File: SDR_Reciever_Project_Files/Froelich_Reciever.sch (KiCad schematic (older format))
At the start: 84 parts, among them J1 I_IN0, J10 LO_I, J11 4.3V, J12 CLK0, J13 RF_IN, J14 RF_OUT, J15 Antenna In, J16 CLK1, J17 CLK2, J18 Conn_01x02_Female, J19 Conn_01x02_Female, J2 I_AMP, J20 I_OUT, J21 Q_OUT, J3 I_IN180, J4 AudioJack3, J5 Q_IN90, J6 Q_AMP, J7 Q_IN270, J8 LO_Q, J9 5V, Q1 PN2222A, U1 INA821ID, U2 SN74CBT3253, U3 OP213FPZ, U4 INA821ID, U5 74AC74, U6 Si5351A-B-GT, U7 LM741, Y1 ATS250

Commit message: Updated footprint libraries, and netlist.
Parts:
- U1, U4: footprint INA821ID:SOIC127P600X175-8N -> Imported_Footprints:INA821ID
- U3: footprint footprints:OP213FPZ -> Imported_Footprints:OP213
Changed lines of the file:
@@
 F 0 "U4" H 5600 3350 50  0000 L CNN
 F 1 "INA821ID" H 5500 3250 50  0000 L CNN
-F 2 "INA821ID:SOIC127P600X175-8N" H 5750 3275 50  0001 L BNN
+F 2 "Imported_Footprints:INA821ID" H 5750 3275 50  0001 L BNN
 F 3 "B" H 5750 3275 50  0001 L BNN
 F 4 "1.75mm" H 5750 3275 50  0001 L BNN "Field4"
@@
 F 0 "U1" H 5600 1875 50  0000 L CNN
 F 1 "INA821ID" H 5500 1775 50  0000 L CNN
-F 2 "INA821ID:SOIC127P600X175-8N" H 5750 1800 50  0001 L BNN
+F 2 "Imported_Footprints:INA821ID" H 5750 1800 50  0001 L BNN
 F 3 "http://www.ti.com/general/docs/suppproductinfo.tsp?distId=10&gotoUrl=http%3A%2F%2Fwww.ti.com%2Flit%2Fgpn%2Fina821" H 5750 1800 50  0001 L BNN
 F 4 "1.75mm" H 5750 1800 50  0001 L BNN "Field4"
@@
 F 0 "U3" H 8600 2375 60  0000 C CNN
 F 1 "OP213FPZ" H 8600 2275 60  0000 C CNN
-F 2 "footprints:OP213FPZ" H 8525 2625 60  0001 C CNN
+F 2 "Imported_Footprints:OP213" H 8525 2625 60  0001 C CNN
 F 3 "" H 7700 3550 60  0000 C CNN
 	1    8050 2325
@@
 J18 and J19 used to test and \nset desired gain.
 $Comp
-L +4.3v:+4.3V #PWR?
+L +4.3v:+4.3V #PWR0102
 U 1 1 5EE28BB2
 P 9850 4050
-F 0 "#PWR?" H 9850 3900 50  0001 C CNN
+F 0 "#PWR0102" H 9850 3900 50  0001 C CNN
 F 1 "+4.3V" H 9865 4223 50  0000 C CNN
 F 2 "" H 9850 4050 50  0001 C CNN

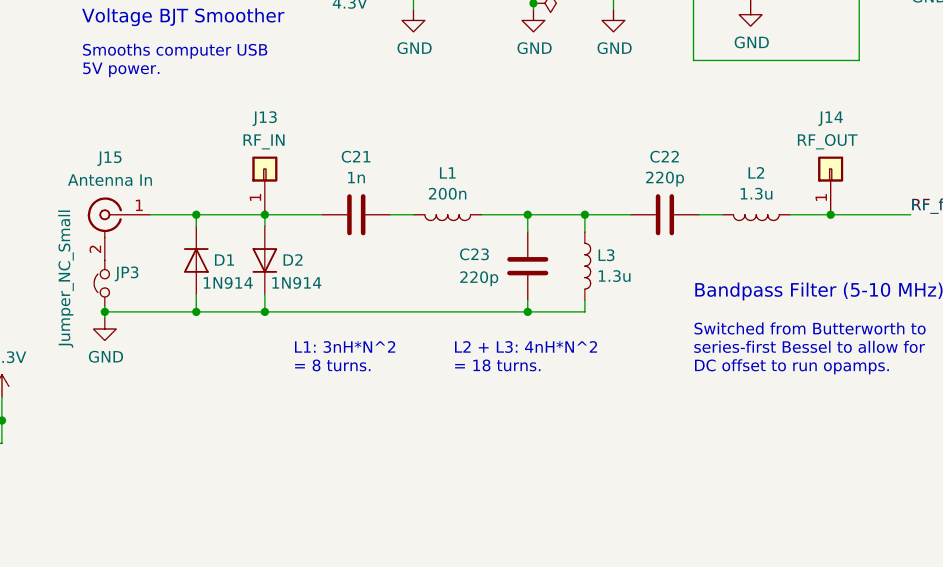
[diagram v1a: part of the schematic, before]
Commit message: Fixed bandpass filter values for v3a.
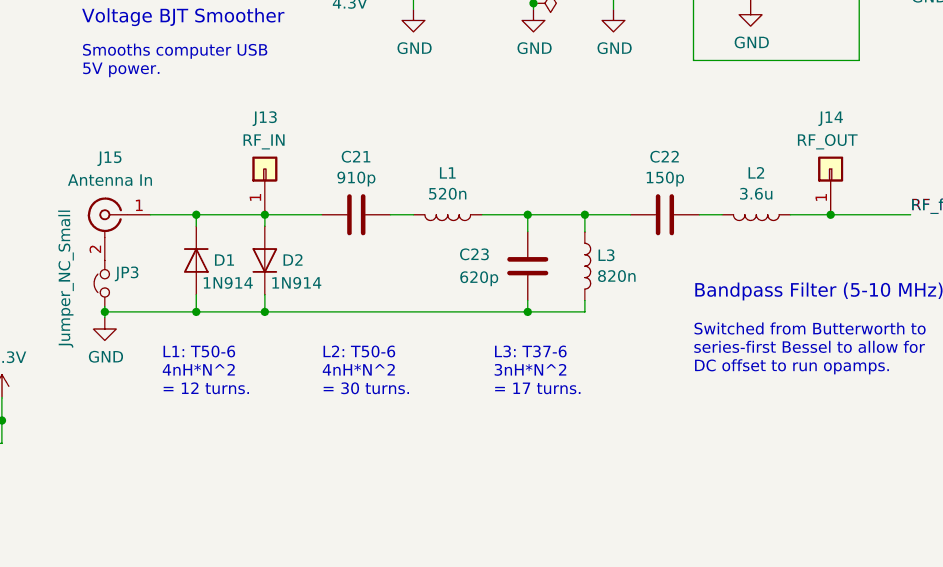
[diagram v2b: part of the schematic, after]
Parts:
- C21: value 1n -> 910p
- C22: value 220p -> 150p
- C23: value 220p -> 620p
- L1: value 200n -> 520n
- L2: value 1.3u -> 3.6u
- L3: value 1.3u -> 820n
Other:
- note added: "L1: T50-6\n4nH*N^2\n= 12 turns."
- note added: "L2: T50-6\n4nH*N^2\n= 30 turns."
- note added: "L3: T37-6\n3nH*N^2\n= 17 turns."
- note removed: "L1: 3nH*N^2\n= 8 turns."
- note removed: "L2 + L3: 4nH*N^2\n= 18 turns."
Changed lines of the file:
@@
 P 9475 5600
 F 0 "C22" V 9223 5600 50  0000 C CNN
-F 1 "220p" V 9314 5600 50  0000 C CNN
+F 1 "150p" V 9314 5600 50  0000 C CNN
 F 2 "Capacitor_THT:C_Disc_D7.0mm_W2.5mm_P5.00mm" H 9513 5450 50  0001 C CNN
 F 3 "~" H 9475 5600 50  0001 C CNN
@@
 P 9875 5600
 F 0 "L2" V 9694 5600 50  0000 C CNN
-F 1 "1.3u" V 9785 5600 50  0000 C CNN
+F 1 "3.6u" V 9785 5600 50  0000 C CNN
 F 2 "Inductor_THT:L_Toroid_Vertical_L13.0mm_W6.5mm_P5.60mm" H 9875 5600 50  0001 C CNN
 F 3 "~" H 9875 5600 50  0001 C CNN
@@
 P 8125 5600
 F 0 "C21" V 7873 5600 50  0000 C CNN
-F 1 "1n" V 7964 5600 50  0000 C CNN
+F 1 "910p" V 7964 5600 50  0000 C CNN
 F 2 "Capacitor_THT:C_Disc_D5.0mm_W2.5mm_P2.50mm" H 8163 5450 50  0001 C CNN
 F 3 "~" H 8125 5600 50  0001 C CNN
@@
 P 8525 5600
 F 0 "L1" V 8344 5600 50  0000 C CNN
-F 1 "200n" V 8435 5600 50  0000 C CNN
+F 1 "520n" V 8435 5600 50  0000 C CNN
 F 2 "Inductor_THT:L_Toroid_Vertical_L10.0mm_W5.0mm_P5.08mm" H 8525 5600 50  0001 C CNN
 F 3 "~" H 8525 5600 50  0001 C CNN
@@
 P 8875 5825
 F 0 "C23" H 8575 5875 50  0000 L CNN
-F 1 "220p" H 8575 5775 50  0000 L CNN
+F 1 "620p" H 8575 5775 50  0000 L CNN
 F 2 "Capacitor_THT:C_Disc_D4.7mm_W2.5mm_P5.00mm" H 8913 5675 50  0001 C CNN
 F 3 "~" H 8875 5825 50  0001 C CNN
@@
 P 9125 5825
 F 0 "L3" H 9178 5871 50  0000 L CNN
-F 1 "1.3u" H 9178 5780 50  0000 L CNN
+F 1 "820n" H 9178 5780 50  0000 L CNN
 F 2 "Inductor_THT:L_Toroid_Vertical_L13.0mm_W6.5mm_P5.60mm" H 9125 5825 50  0001 C CNN
 F 3 "~" H 9125 5825 50  0001 C CNN
@@
 	1    0    0    -1
 $EndComp
-Text Notes 8550 6300 0    50   ~ 0
-L2 + L3: 4nH*N^2\n= 18 turns.
-Text Notes 7850 6300 0    50   ~ 0
-L1: 3nH*N^2\n= 8 turns.
+Text Notes 7975 6400 0    50   ~ 0
+L2: T50-6\n4nH*N^2\n= 30 turns.
+Text Notes 7275 6400 0    50   ~ 0
+L1: T50-6\n4nH*N^2\n= 12 turns.
 $Comp
 L Amplifier_Operational:OP179GS U7
@@
 	1    0    0    -1
 $EndComp
+Text Notes 8725 6400 0    50   ~ 0
+L3: T37-6\n3nH*N^2\n= 17 turns.
 $EndSCHEMATC
